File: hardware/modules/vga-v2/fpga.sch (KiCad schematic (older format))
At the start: 40 parts, among them J301 Conn_02x05_Odd_Even, SW301 SW_Push, U301 W25Q32JVSS, U302 ICE40HX1K-VQ100, U303 IS63LV1024L, X301 25.175 MHz

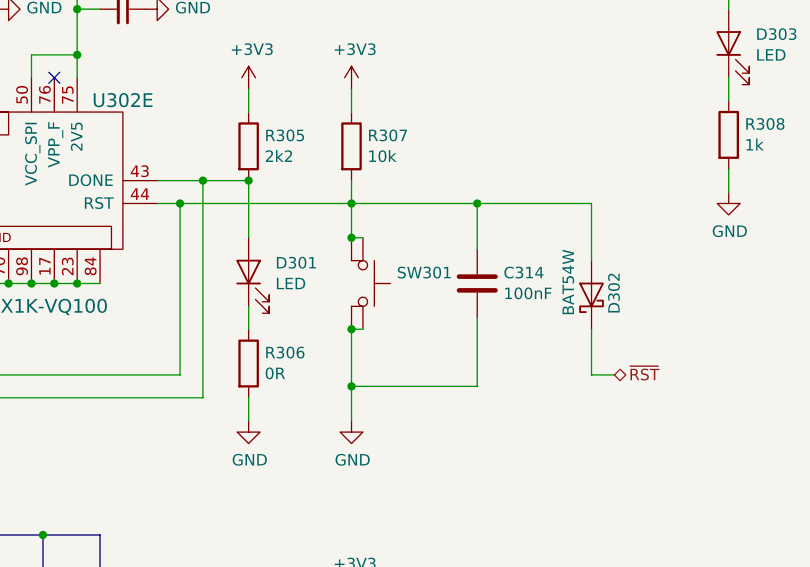
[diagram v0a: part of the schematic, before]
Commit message: Use existing button
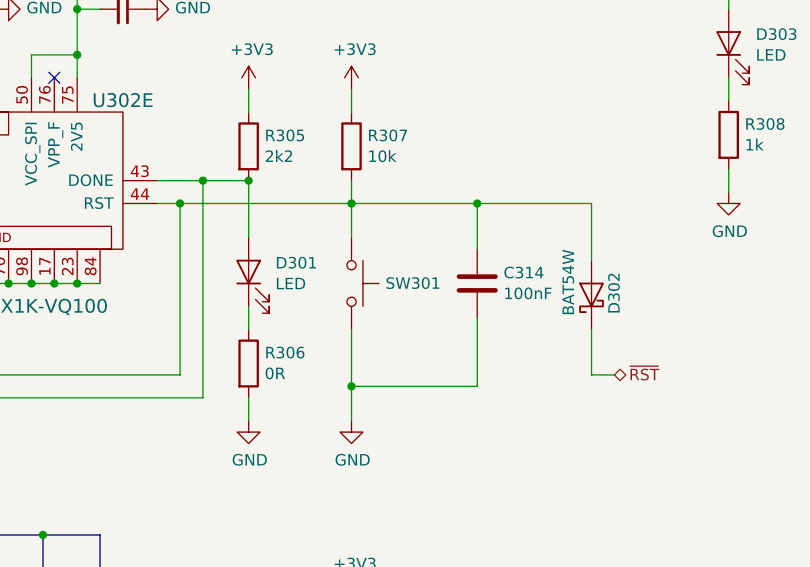
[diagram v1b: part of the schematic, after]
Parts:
- removed SW301: SW_Push, Button_Switch_THT:SW_TH_Tactile_Omron_B3F-10xx, symbol zi28:SW_Push
- added SW301: SW_Push, Button_Switch_THT:SW_PUSH_6mm_H5mm, symbol Switch:SW_Push
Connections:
- net GND: now also SW301.2
- net at C314.1, D302.2 (A), J301.6 (Pin_6)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: now also SW301.1
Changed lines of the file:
@@
 $EndComp
-$Comp
-L zi28:SW_Push SW?
-U 1 1 5E590B46
-P 6600 3050
-AR Path="/5E590B46" Ref="SW?"  Part="1"
-AR Path="/5E4BD7CF/5E590B46" Ref="SW301"  Part="1"
-F 0 "SW301" V 6554 3198 50  0000 L CNN
-F 1 "SW_Push" V 6645 3198 50  0001 L CNN
-F 2 "Button_Switch_THT:SW_TH_Tactile_Omron_B3F-10xx" H 6600 3250 50  0001 C CNN
-F 3 "~" H 6600 3250 50  0001 C CNN
-	1    6600 3050
-	0    1    1    0
-$EndComp
-Wire Wire Line
-	6600 2850 6550 2850
-Connection ~ 6550 2850
-Wire Wire Line
-	6600 3250 6550 3250
-Connection ~ 6550 3250
 $Comp
 L Device:C C?
@@
 Wire Bus Line
 	3000 4150 3000 7100
+$Comp
+L Switch:SW_Push SW301
+U 1 1 5DF8EDA7
+P 6550 3050
+F 0 "SW301" V 6550 3198 50  0000 L CNN
+F 1 "SW_Push" V 6595 3198 50  0001 L CNN
+F 2 "Button_Switch_THT:SW_PUSH_6mm_H5mm" H 6550 3250 50  0001 C CNN
+F 3 "~" H 6550 3250 50  0001 C CNN
+	1    6550 3050
+	0    1    1    0
+$EndComp
 $EndSCHEMATC
